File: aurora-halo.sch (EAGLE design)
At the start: 9 parts

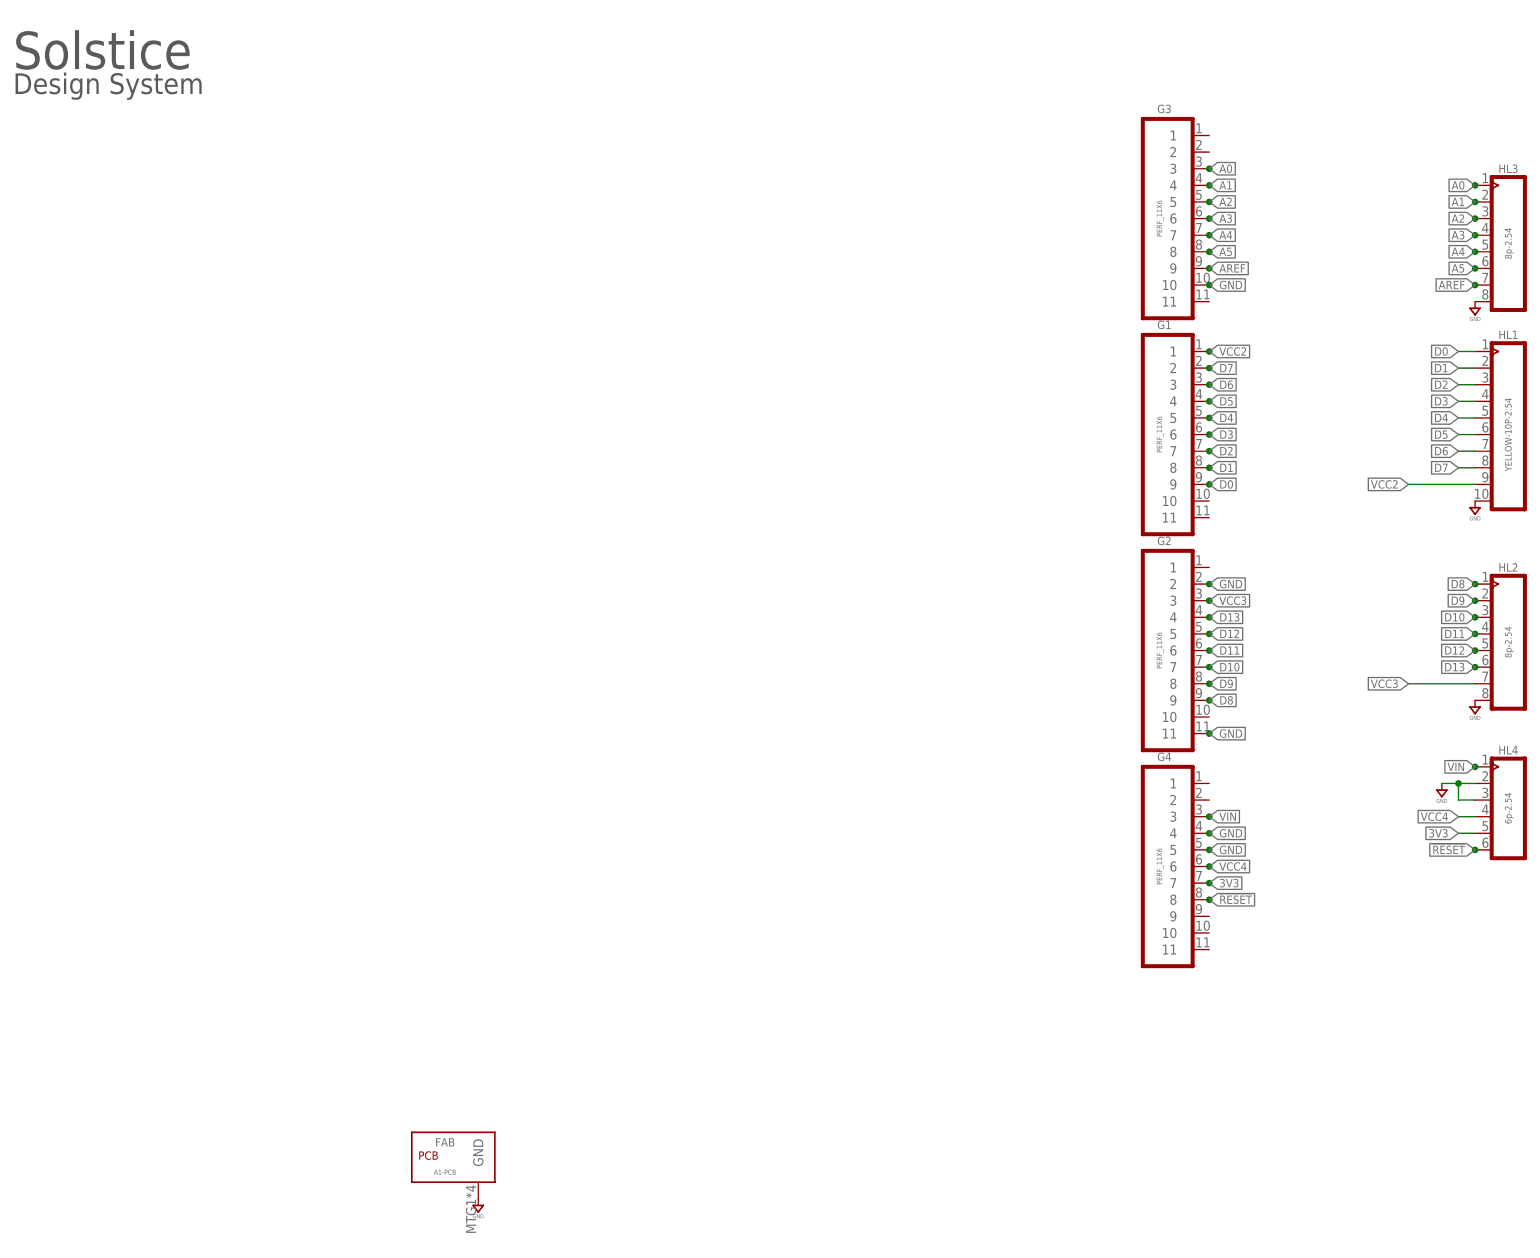
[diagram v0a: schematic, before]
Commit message: Update PCB to Rev. B
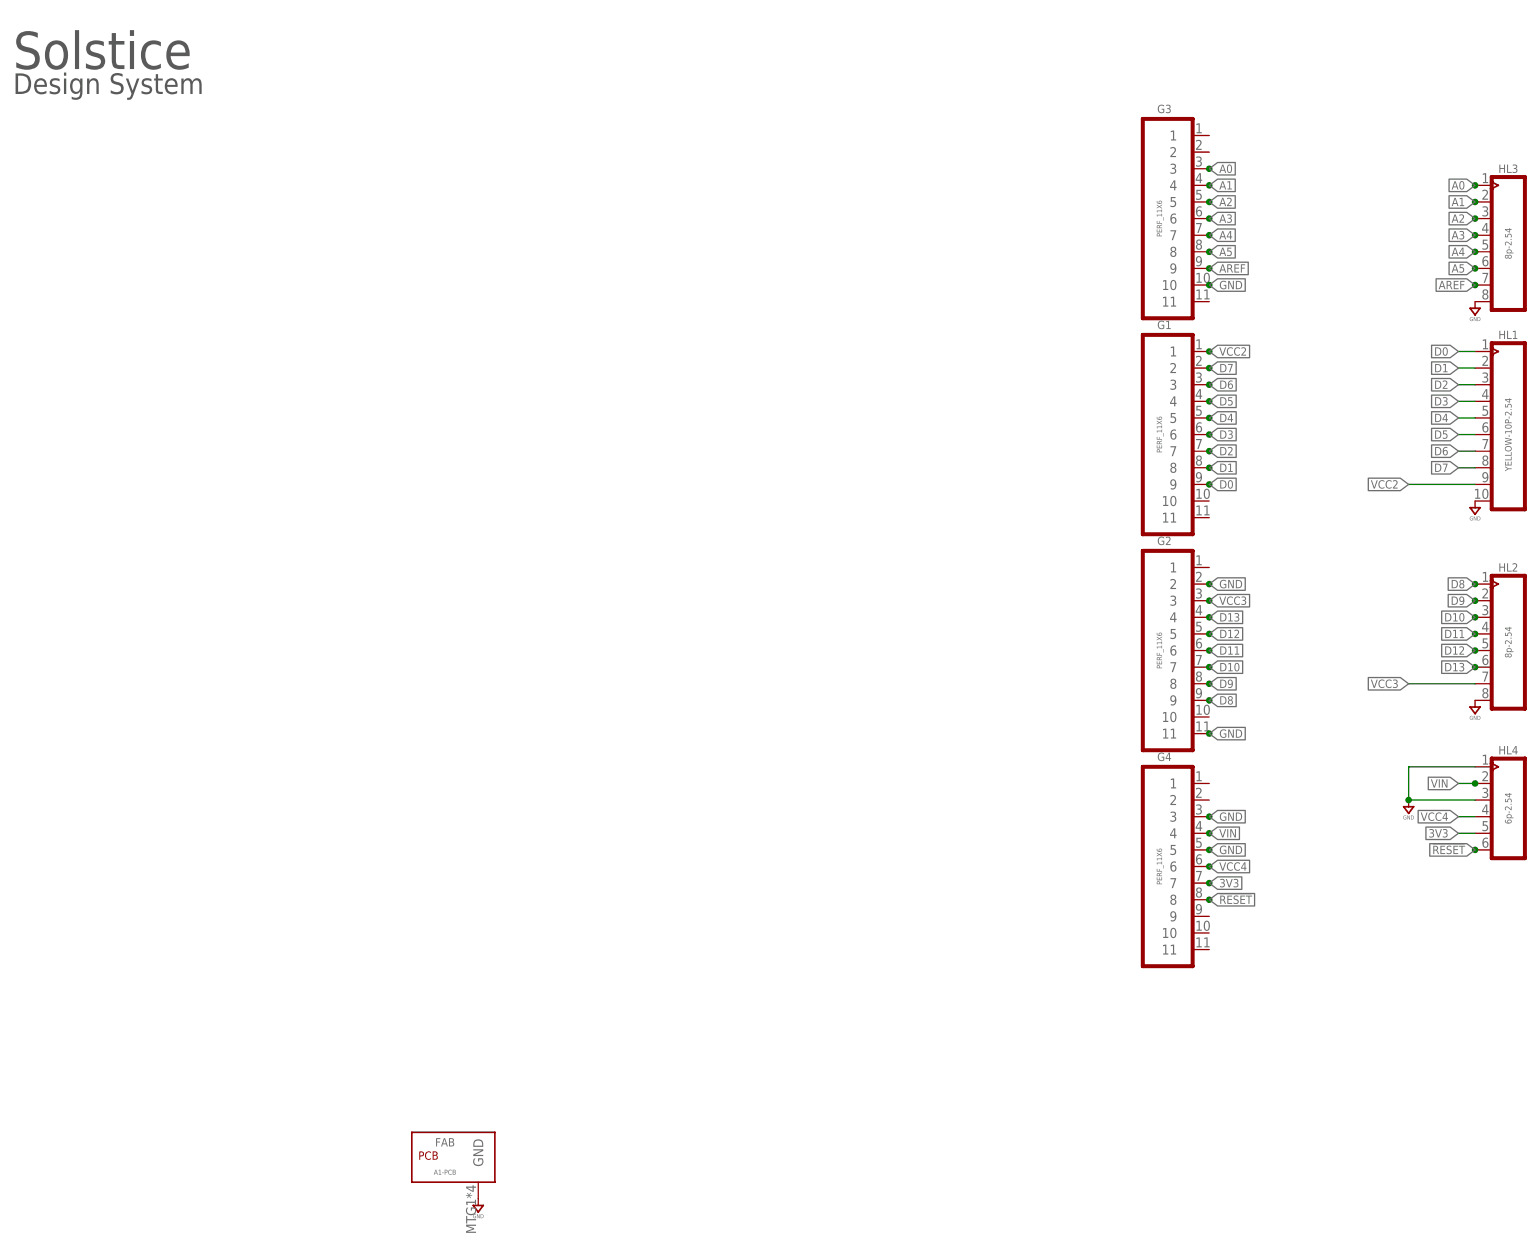
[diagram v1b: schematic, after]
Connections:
- net GND: now also G4.3, HL4.1; no longer G4.4, HL4.2
- net VIN: now also G4.4, HL4.2; no longer G4.3, HL4.1
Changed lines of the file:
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@@
 <?xml version="1.0" encoding="utf-8"?>
 <!DOCTYPE eagle SYSTEM "eagle.dtd">
-<eagle version="9.1.3">
+<eagle version="9.2.2">
 <drawing>
 <settings>
@@
 <parts>
 <part name="U$1" library="frames-custom" deviceset="LETTER_L-CIRCUITMONKEY" device="">
-<attribute name="DOCUMENT_NUMBER" value="0740-Aurora"/>
-<attribute name="REV" value="A"/>
+<attribute name="DOCUMENT_NUMBER" value="Aurora (open source)"/>
+<attribute name="REV" value="B"/>
 </part>
 <part name="HL3" library="Seeed-Connector" deviceset="DIP-BLACK-FEMALE-HEADER-VERT(8P-2.54)" device="" value="8p-2.54"/>
@@
 </plain>
 <instances>
-<instance part="U$1" gate="G$1" x="0" y="0"/>
-<instance part="U$1" gate="G$2" x="147.32" y="0">
-<attribute name="REV" x="147.32" y="0" size="1.778" layer="96" display="off"/>
-<attribute name="DOCUMENT_NUMBER" x="147.32" y="0" size="1.778" layer="96" display="off"/>
-</instance>
-<instance part="HL3" gate="G$1" x="231.14" y="152.4"/>
-<instance part="SUPPLY52" gate="GND" x="226.06" y="142.24"/>
-<instance part="SUPPLY53" gate="GND" x="226.06" y="111.76"/>
-<instance part="HL2" gate="G$1" x="231.14" y="91.44"/>
-<instance part="SUPPLY56" gate="GND" x="226.06" y="81.28"/>
-<instance part="HL1" gate="G$1" x="231.14" y="121.92"/>
-<instance part="HL4" gate="G$1" x="231.14" y="66.04"/>
-<instance part="SUPPLY54" gate="GND" x="220.98" y="68.58"/>
-<instance part="FAB" gate="G$1" x="68.58" y="10.16"/>
-<instance part="SUPPLY58" gate="GND" x="73.66" y="5.08"/>
-<instance part="G1" gate="G$1" x="177.8" y="124.46"/>
-<instance part="G2" gate="G$1" x="177.8" y="91.44"/>
-<instance part="G3" gate="G$1" x="177.8" y="157.48"/>
-<instance part="G4" gate="G$1" x="177.8" y="58.42"/>
+<instance part="U$1" gate="G$1" x="0" y="0" smashed="yes"/>
+<instance part="U$1" gate="G$2" x="147.32" y="0" smashed="yes">
+<attribute name="LAST_DATE_TIME" x="160.02" y="1.27" size="2.54" layer="94" font="vector"/>
+<attribute name="SHEET" x="233.68" y="1.27" size="2.54" layer="94" font="vector"/>
+<attribute name="DRAWING_NAME" x="91.44" y="1.27" size="2.54" layer="94" font="vector" ratio="15"/>
+<attribute name="DOCUMENT_NUMBER" x="160.02" y="6.096" size="3.81" layer="94" ratio="15"/>
+<attribute name="REV" x="241.808" y="8.382" size="3.81" layer="94" ratio="15" align="center"/>
+</instance>
+<instance part="HL3" gate="G$1" x="231.14" y="152.4" smashed="yes">
+<attribute name="NAME" x="231.14" y="162.56" size="1.27" layer="95" font="vector" ratio="15" align="center"/>
+<attribute name="VALUE" x="231.14" y="151.13" size="1.016" layer="96" font="vector" ratio="10" rot="R90" align="center"/>
+</instance>
+<instance part="SUPPLY52" gate="GND" x="226.06" y="142.24" smashed="yes">
+<attribute name="VALUE" x="226.06" y="139.573" size="0.6096" layer="96" font="vector" align="center"/>
+</instance>
+<instance part="SUPPLY53" gate="GND" x="226.06" y="111.76" smashed="yes">
+<attribute name="VALUE" x="226.06" y="109.093" size="0.6096" layer="96" font="vector" align="center"/>
+</instance>
+<instance part="HL2" gate="G$1" x="231.14" y="91.44" smashed="yes">
+<attribute name="NAME" x="231.14" y="101.6" size="1.27" layer="95" font="vector" ratio="15" align="center"/>
+<attribute name="VALUE" x="231.14" y="90.17" size="1.016" layer="96" font="vector" ratio="10" rot="R90" align="center"/>
+</instance>
+<instance part="SUPPLY56" gate="GND" x="226.06" y="81.28" smashed="yes">
+<attribute name="VALUE" x="226.06" y="78.613" size="0.6096" layer="96" font="vector" align="center"/>
+</instance>
+<instance part="HL1" gate="G$1" x="231.14" y="121.92" smashed="yes">
+<attribute name="NAME" x="231.14" y="137.16" size="1.27" layer="95" ratio="15" align="center"/>
+<attribute name="VALUE" x="231.14" y="121.92" size="1.016" layer="95" ratio="10" rot="R90" align="center"/>
+</instance>
+<instance part="HL4" gate="G$1" x="231.14" y="66.04" smashed="yes">
+<attribute name="NAME" x="231.14" y="73.66" size="1.27" layer="95" ratio="15" align="center"/>
+<attribute name="VALUE" x="231.14" y="64.77" size="1.016" layer="96" ratio="10" rot="R90" align="center"/>
+</instance>
+<instance part="SUPPLY54" gate="GND" x="215.9" y="66.04" smashed="yes">
+<attribute name="VALUE" x="215.9" y="63.373" size="0.6096" layer="96" font="vector" align="center"/>
+</instance>
+<instance part="FAB" gate="G$1" x="68.58" y="10.16" smashed="yes">
+<attribute name="NAME" x="68.58" y="13.716" size="1.27" layer="95" font="vector" ratio="15" align="center"/>
+<attribute name="VALUE" x="68.58" y="9.144" size="0.762" layer="95" font="vector" align="center"/>
+</instance>
+<instance part="SUPPLY58" gate="GND" x="73.66" y="5.08" smashed="yes">
+<attribute name="VALUE" x="73.66" y="2.413" size="0.6096" layer="96" font="vector" align="center"/>
+</instance>
+<instance part="G1" gate="G$1" x="177.8" y="124.46" smashed="yes">
+<attribute name="VALUE" x="177.8" y="121.92" size="0.8128" layer="96" font="vector" rot="R90" align="center"/>
+<attribute name="NAME" x="178.562" y="138.684" size="1.27" layer="95" font="vector" ratio="15" align="center"/>
+</instance>
+<instance part="G2" gate="G$1" x="177.8" y="91.44" smashed="yes">
+<attribute name="VALUE" x="177.8" y="88.9" size="0.8128" layer="96" font="vector" rot="R90" align="center"/>
+<attribute name="NAME" x="178.562" y="105.664" size="1.27" layer="95" font="vector" ratio="15" align="center"/>
+</instance>
+<instance part="G3" gate="G$1" x="177.8" y="157.48" smashed="yes">
+<attribute name="VALUE" x="177.8" y="154.94" size="0.8128" layer="96" font="vector" rot="R90" align="center"/>
+<attribute name="NAME" x="178.562" y="171.704" size="1.27" layer="95" font="vector" ratio="15" align="center"/>
+</instance>
+<instance part="G4" gate="G$1" x="177.8" y="58.42" smashed="yes">
+<attribute name="VALUE" x="177.8" y="55.88" size="0.8128" layer="96" font="vector" rot="R90" align="center"/>
+<attribute name="NAME" x="178.562" y="72.644" size="1.27" layer="95" font="vector" ratio="15" align="center"/>
+</instance>
 </instances>
 <busses>
@@
 <segment>
 <pinref part="SUPPLY54" gate="GND" pin="GND"/>
-<pinref part="HL4" gate="G$1" pin="2"/>
-<wire x1="226.06" y1="68.58" x2="223.52" y2="68.58" width="0.1524" layer="91"/>
 <pinref part="HL4" gate="G$1" pin="3"/>
-<wire x1="223.52" y1="68.58" x2="220.98" y2="68.58" width="0.1524" layer="91"/>
-<wire x1="226.06" y1="66.04" x2="223.52" y2="66.04" width="0.1524" layer="91"/>
-<wire x1="223.52" y1="66.04" x2="223.52" y2="68.58" width="0.1524" layer="91"/>
-<junction x="223.52" y="68.58"/>
+<wire x1="226.06" y1="66.04" x2="215.9" y2="66.04" width="0.1524" layer="91"/>
+<pinref part="HL4" gate="G$1" pin="1"/>
+<wire x1="226.06" y1="71.12" x2="215.9" y2="71.12" width="0.1524" layer="91"/>
+<wire x1="215.9" y1="71.12" x2="215.9" y2="66.04" width="0.1524" layer="91"/>
+<junction x="215.9" y="66.04"/>
 </segment>
 <segment>
@@
 </segment>
 <segment>
+<pinref part="G4" gate="G$1" pin="5"/>
+<junction x="185.42" y="58.42"/>
+<label x="185.42" y="58.42" size="1.27" layer="95" xref="yes"/>
+</segment>
+<segment>
+<pinref part="G4" gate="G$1" pin="3"/>
+<junction x="185.42" y="63.5"/>
+<label x="185.42" y="63.5" size="1.27" layer="95" xref="yes"/>
+</segment>
+</net>
+<net name="AREF" class="0">
+<segment>
+<pinref part="HL3" gate="G$1" pin="7"/>
+<junction x="226.06" y="144.78"/>
+<label x="226.06" y="144.78" size="1.27" layer="95" rot="R180" xref="yes"/>
+</segment>
+<segment>
+<pinref part="G3" gate="G$1" pin="9"/>
+<junction x="185.42" y="147.32"/>
+<label x="185.42" y="147.32" size="1.27" layer="95" xref="yes"/>
+</segment>
+</net>
+<net name="VIN" class="0">
+<segment>
+<pinref part="HL4" gate="G$1" pin="2"/>
+<wire x1="226.06" y1="68.58" x2="223.52" y2="68.58" width="0.1524" layer="91"/>
+<label x="223.52" y="68.58" size="1.27" layer="95" rot="R180" xref="yes"/>
+<junction x="226.06" y="68.58"/>
+</segment>
+<segment>
 <pinref part="G4" gate="G$1" pin="4"/>
 <junction x="185.42" y="60.96"/>
 <label x="185.42" y="60.96" size="1.27" layer="95" xref="yes"/>
 </segment>
-<segment>
-<pinref part="G4" gate="G$1" pin="5"/>
-<junction x="185.42" y="58.42"/>
-<label x="185.42" y="58.42" size="1.27" layer="95" xref="yes"/>
-</segment>
 </net>
-<net name="AREF" class="0">
-<segment>
-<pinref part="HL3" gate="G$1" pin="7"/>
-<junction x="226.06" y="144.78"/>
-<label x="226.06" y="144.78" size="1.27" layer="95" rot="R180" xref="yes"/>
-</segment>
-<segment>
-<pinref part="G3" gate="G$1" pin="9"/>
-<junction x="185.42" y="147.32"/>
-<label x="185.42" y="147.32" size="1.27" layer="95" xref="yes"/>
-</segment>
-</net>
-<net name="VIN" class="0">
-<segment>
-<pinref part="HL4" gate="G$1" pin="1"/>
-<junction x="226.06" y="71.12"/>
-<label x="226.06" y="71.12" size="1.27" layer="95" font="vector" rot="R180" xref="yes"/>
-</segment>
-<segment>
-<pinref part="G4" gate="G$1" pin="3"/>
-<junction x="185.42" y="63.5"/>
-<label x="185.42" y="63.5" size="1.27" layer="95" xref="yes"/>
-</segment>
-</net>
